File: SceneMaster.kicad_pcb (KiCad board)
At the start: 4 copper layers, 50 x 30 mm, 107 parts, among them J1 TYPE-C-31-M-12, J10 Conn_01x08_Male, J11 PowerIn, J12 PowerOut, J13 LED3, J14 LED4, J15 LED5, J2 SPK_R, J3 LED1, J4 LED2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

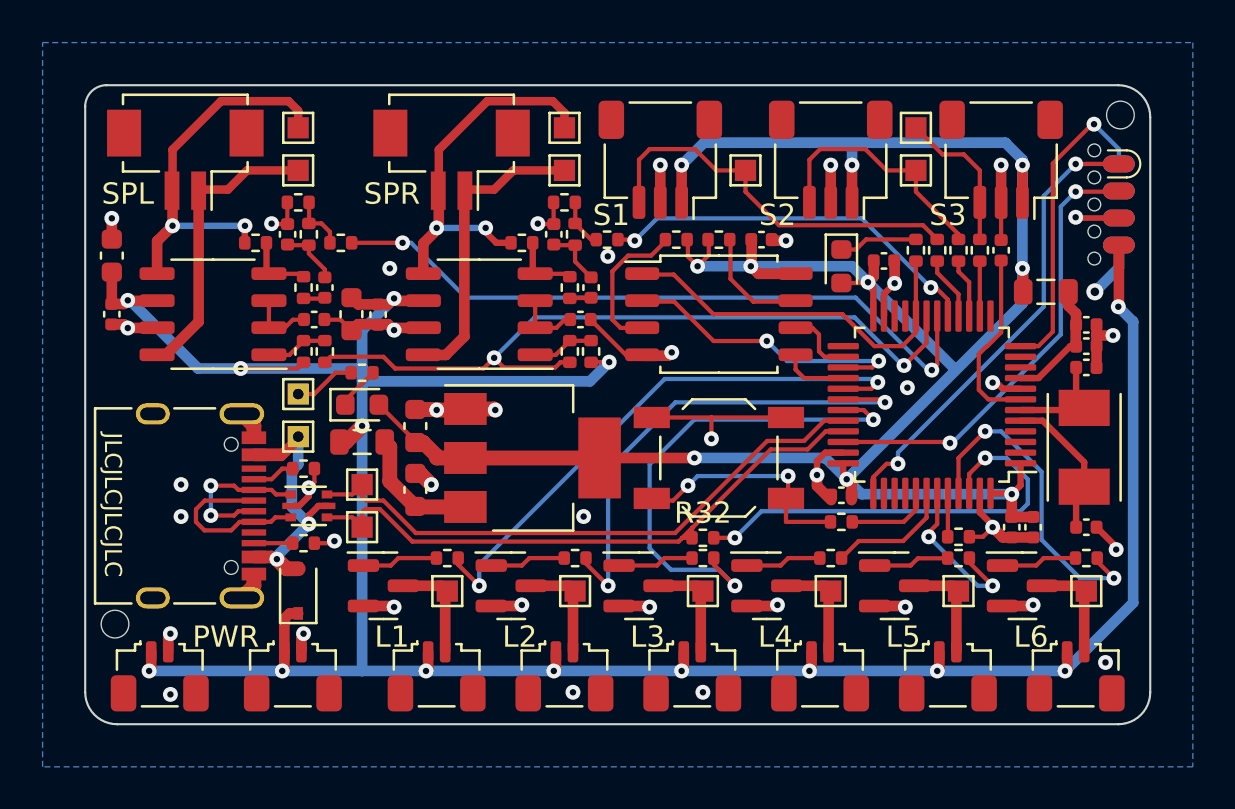
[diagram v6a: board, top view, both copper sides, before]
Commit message: Change programming port
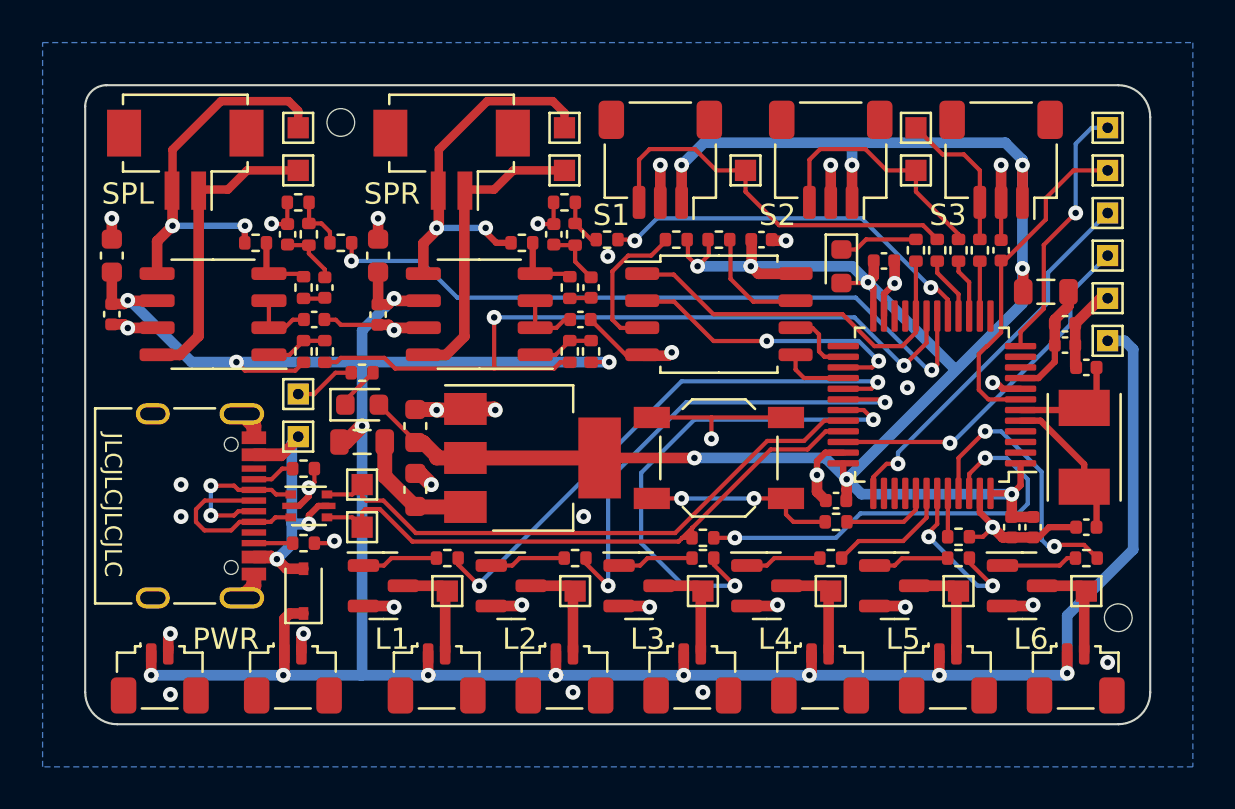
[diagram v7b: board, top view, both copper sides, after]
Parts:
- removed J10: Conn_01x08_Male, ant:SOIC_clipProgSmall
- added TP19: 5V, TestPoint:TestPoint_THTPad_1.0x1.0mm_Drill0.5mm, F.Cu at (148.0, 77.0)
- added TP20: GND, TestPoint:TestPoint_THTPad_1.0x1.0mm_Drill0.5mm, F.Cu at (148.0, 75.0)
- added TP23: NRST, TestPoint:TestPoint_THTPad_1.0x1.0mm_Drill0.5mm, F.Cu at (148.0, 69.0)
- added TP3: SWDIO, TestPoint:TestPoint_THTPad_1.0x1.0mm_Drill0.5mm, F.Cu at (148.0, 73.0)
- added TP4: SWCLK, TestPoint:TestPoint_THTPad_1.0x1.0mm_Drill0.5mm, F.Cu at (148.0, 71.0)
- added TP5: UARTTX, TestPoint:TestPoint_THTPad_1.0x1.0mm_Drill0.5mm, F.Cu at (148.0, 67.0)
- C10, C8: value 2.2u -> 470n
- R12, R13, R15, R16, R17, R18, R22, R26, R27, R28, R29, R3, R30, R31, R32, R4, R5, R6, R7: value 1k -> 1k5
- R21, R25: value 20k -> 33k
- moved REF** 47.1 mm to (148.5, 90.0)
- moved REF** 36.6 mm to (112.0, 66.8)
- moved C21 3.02 mm to (113.8, 73.0), turned to 90 degrees
- moved C12 1.00 mm to (146.0, 76.2)
- moved C7 1.00 mm to (146.0, 77.2)
- moved C3 0.35 mm to (135.2, 84.5)
- moved D1 0.25 mm to (110.2, 88.8)
- moved R3 0.25 mm to (135.2, 85.5)
- moved J11 0.10 mm to (103.5, 92.8)
- moved J12 0.10 mm to (109.8, 92.8)
- moved J13 0.10 mm to (128.5, 92.8)
- moved J14 0.10 mm to (134.5, 92.8)
- moved J15 0.10 mm to (140.5, 92.8)
- moved J3 0.10 mm to (116.5, 92.8)
- moved J4 0.10 mm to (122.5, 92.8)
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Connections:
- net Net-(C15-Pad2) renamed /NRST
- C10 pad 1: Net-(C10-Pad1) -> /Line_Out_L
- C10 pad 2: /Line_Out_L -> Net-(C10-Pad2)
- C11 pad 1: Net-(C10-Pad1) -> /Line_Out_L
- C8 pad 1: Net-(C8-Pad1) -> /Line_Out_R
- C8 pad 2: /Line_Out_R -> Net-(C8-Pad2)
- C9 pad 1: Net-(C8-Pad1) -> /Line_Out_R
- R20 pad 2: /Line_Out_R -> Net-(C8-Pad2)
- R24 pad 2: /Line_Out_L -> Net-(C10-Pad2)
- R8 pad 2: Net-(C8-Pad1) -> /Line_Out_R
- R9 pad 2: Net-(C10-Pad1) -> /Line_Out_L
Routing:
- net /NRST: track 8.67 -> 16.0 mm
- net /SWDIO: track 21.4 -> 16.9 mm, vias 2 -> 1
- net /SWCLK: track 21.7 -> 18.0 mm, vias 2 -> 1
- net Net-(C8-Pad1): track 2.80 -> 0.00 mm
- net Net-(C10-Pad1): track 2.79 -> 0.00 mm
- net +5V: track 130.3 -> 127.8 mm, vias 14 -> 13
- net /LED6: track 15.5 -> 13.1 mm
- net /UART_TX: track 14.7 -> 12.4 mm
- net Net-(R3-Pad1): track 11.1 -> 9.04 mm
- net GND: track 73.7 -> 71.6 mm, vias 42 -> 38
- net /Line_Out_R: track 0.97 -> 2.80 mm
- net /Line_Out_L: track 0.97 -> 2.79 mm
- net /MUTE: track 36.0 -> 37.2 mm
- net /VBUS: track 15.9 -> 17.0 mm
- net Net-(C8-Pad2): track 0.00 -> 0.97 mm
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
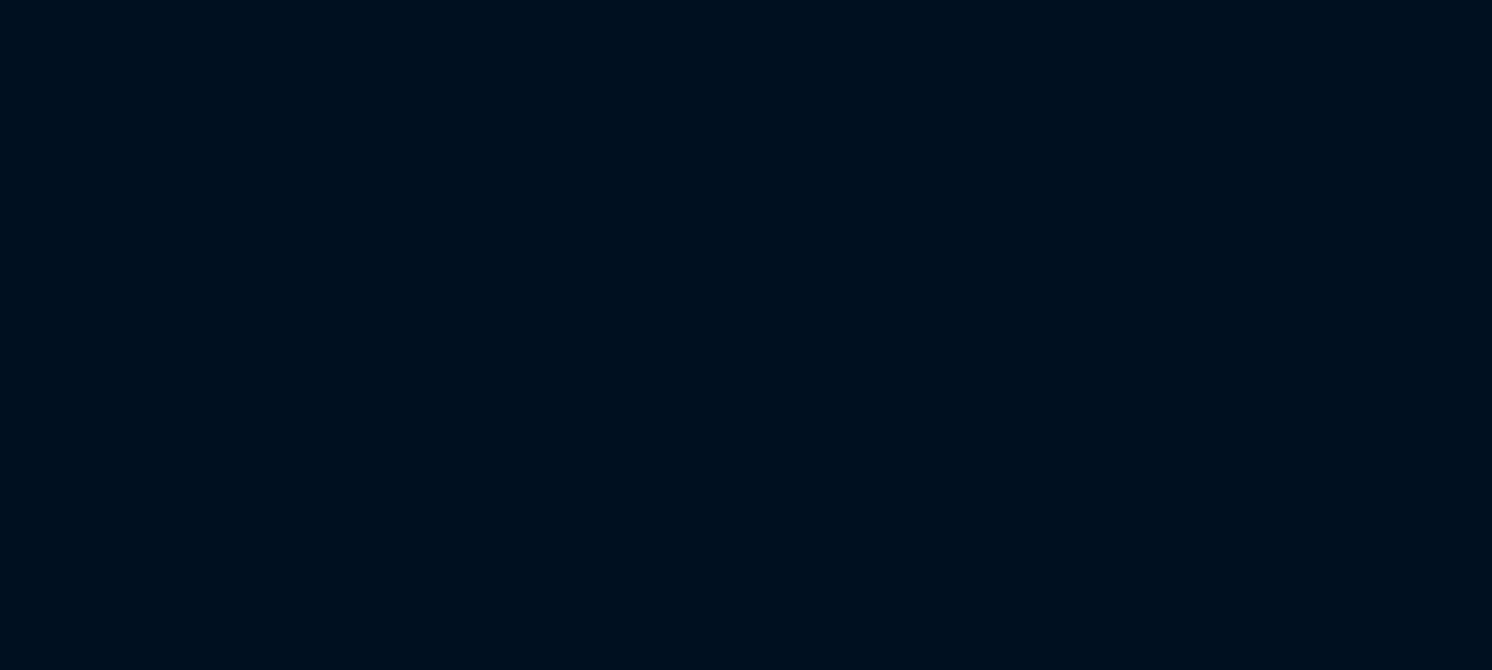
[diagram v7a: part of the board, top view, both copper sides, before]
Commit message: add license
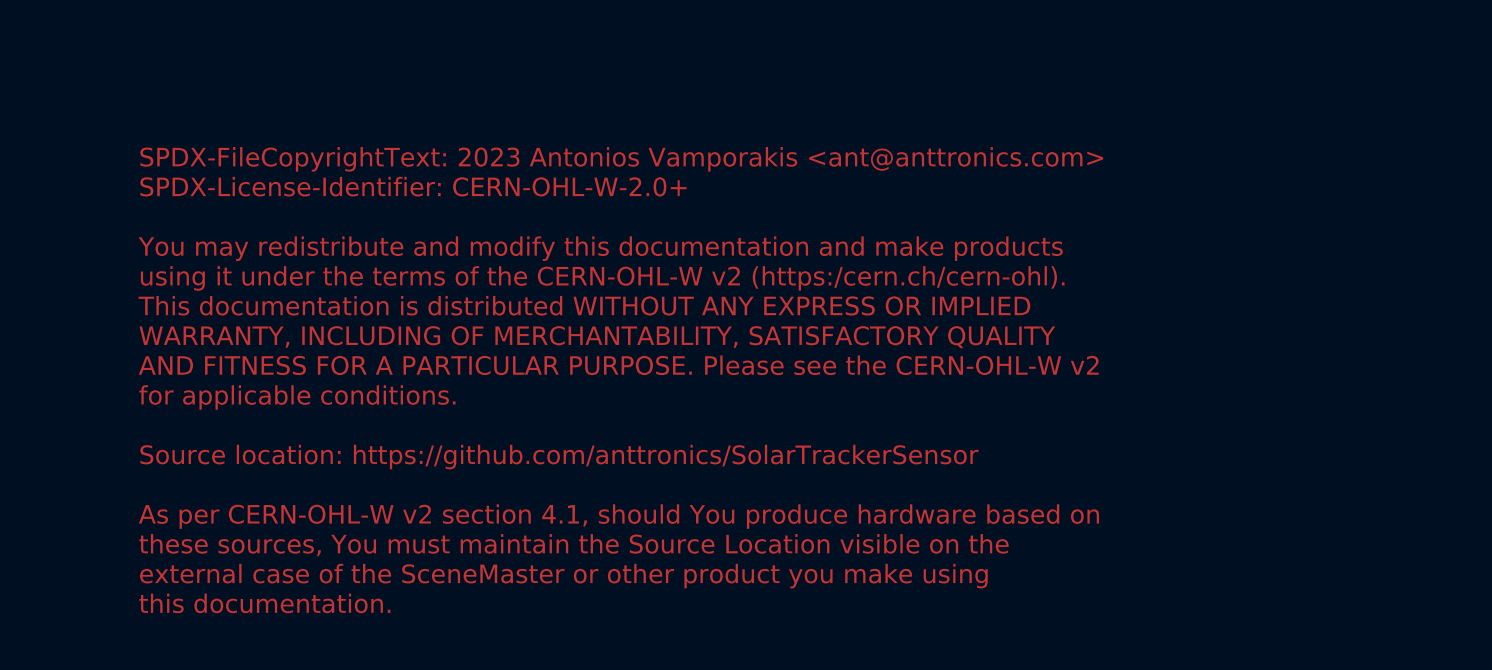
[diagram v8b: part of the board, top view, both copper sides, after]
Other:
- board text added: "SPDX-FileCopyrightText: 2023 Antonios Vamporakis <ant@anttronics.com> SPDX-License-Identifier: CERN-OHL-W-2.0+ You may redistribute and modify this documentation and make products using it under the terms of the CERN-OHL-W v2 (https:/cern.ch/cern-ohl). This documentation is distributed WITHOUT ANY EXPRESS OR IMPLIED WARRANTY, INCLUDING OF MERCHANTABILITY, SATISFACTORY QUALITY AND FITNESS FOR A PA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"
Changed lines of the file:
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@@
   )
   (paper "A4")
+  (title_block
+    (title "SceneMaster")
+    (date "2023-12-21")
+    (rev "0.1")
+    (company "AntTronics")
+  )
   (layers
     (0 "F.Cu" signal)
@@
   (gr_line (start 101.5 95) (end 148.5 95) (layer "Edge.Cuts") (width 0.1))
   (gr_arc (start 101.5 95) (mid 100.43934 94.56066) (end 100 93.5) (layer "Edge.Cuts") (width 0.1))
+  (gr_text "SPDX-FileCopyrightText: 2023 Antonios Vamporakis <ant@anttronics.com>\nSPDX-License-Identifier: CERN-OHL-W-2.0+\n\nYou may redistribute and modify this documentation and make products\nusing it under the terms of the CERN-OHL-W v2 (https:/cern.ch/cern-ohl).\nThis documentation is distributed WITHOUT ANY EXPRESS OR IMPLIED\nWARRANTY, INCLUDING OF MERCHANTABILITY, SATISFACTORY QUALITY\nAND FITNESS FOR A PARTICULAR PURPOSE. Please see the CERN-OHL-W v2\nfor applicable conditions.\n\nSource location: https://github.com/anttronics/SolarTrackerSensor\n\nAs per CERN-OHL-W v2 section 4.1, should You produce hardware based on\nthese sources, You must maintain the Source Location visible on the\nexternal case of the SceneMaster or other product you make using\nthis documentation.\n" (at 236 177) (layer "F.Cu")
+    (effects (font (size 0.8 0.8) (thickness 0.15)) (justify left))
+  )
   (gr_text "SceneMaster" (at 102 68.5 180) (layer "B.SilkS")
     (effects (font (size 1.5 1.5) (thickness 0.2)) (justify left mirror))
